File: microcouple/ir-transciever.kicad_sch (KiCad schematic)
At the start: 4 parts, among them U8 TSOP34138

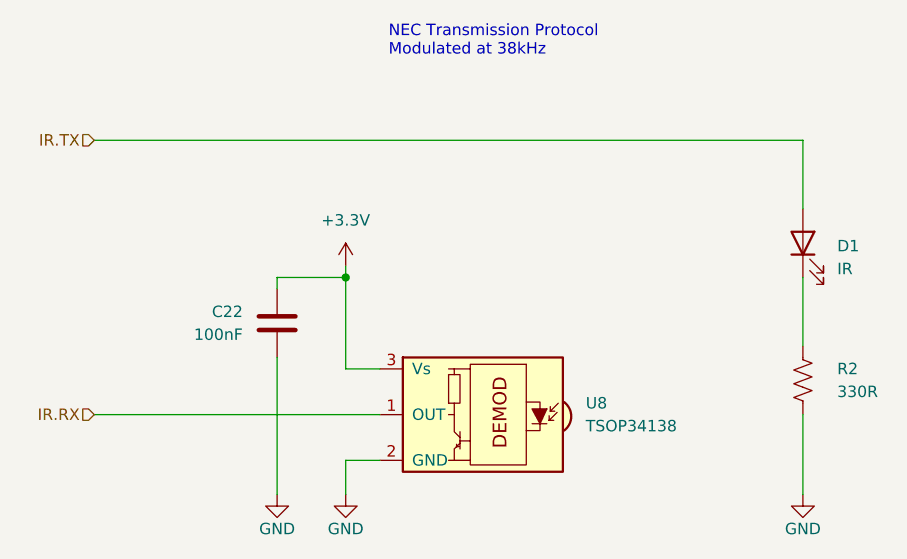
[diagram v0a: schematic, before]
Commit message: Switch THT IR components to SMD ones
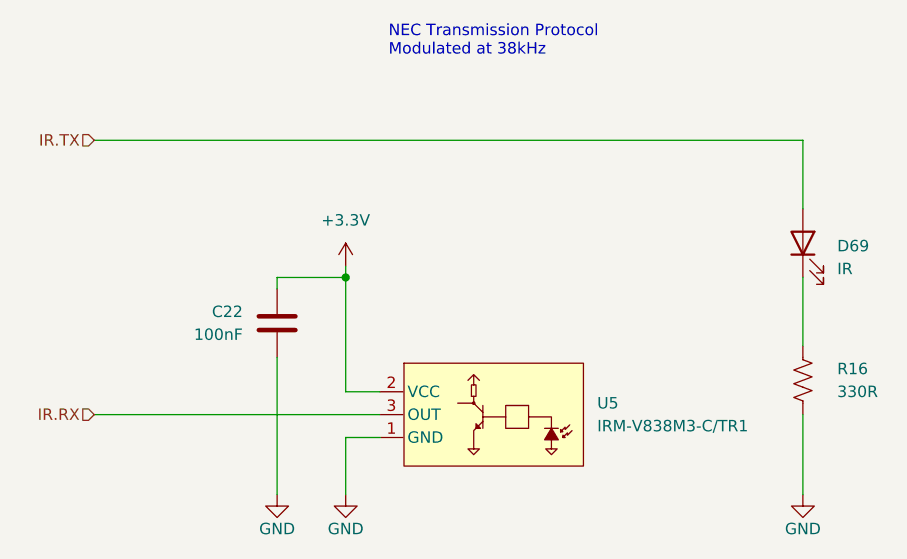
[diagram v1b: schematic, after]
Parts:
- removed U8: TSOP34138, OptoDevice:Vishay_MOLD-3Pin, symbol Interface_Optical:TSOP341xx
- added U5: IRM-V838M3-C/TR1, easyeda2kicad:OPTO-SMD_IRM-V838M3-C-TR1, symbol GS_Optoelectronic:IRM-V838M3-C_TR1
- D69: renamed from D1; footprint LED_THT:LED_SideEmitter_Rectangular_W4.5mm_H1.6mm -> easyeda2kicad:LED-SMD_L3.0-W2.7-RD; LCSC ID (none) -> C181893
- renumbered R2 to R16
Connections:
- net +3.3V: now also U5.2 (VCC)
- net GND: now also U5.1 (GND), U5.4 (GND)
- net IR.RX: now also U5.3 (OUT)
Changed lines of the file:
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@@
 	(wire
 		(pts
-			(xy 71.12 83.82) (xy 74.93 83.82)
-		)
-		(stroke
-			(width 0)
-			(type default)
-		)
-	)
-	(wire
-		(pts
-			(xy 71.12 87.63) (xy 71.12 83.82)
+			(xy 71.12 81.28) (xy 74.93 81.28)
+		)
+		(stroke
+			(width 0)
+			(type default)
+		)
+	)
+	(wire
+		(pts
+			(xy 71.12 87.63) (xy 71.12 81.28)
 		)
 		(stroke
@@
 	(wire
 		(pts
-			(xy 71.12 63.5) (xy 71.12 73.66)
+			(xy 71.12 63.5) (xy 71.12 76.2)
 		)
 		(stroke
@@
 	(wire
 		(pts
-			(xy 71.12 73.66) (xy 74.93 73.66)
+			(xy 71.12 76.2) (xy 74.93 76.2)
 		)
 		(stroke
@@
 	)
 	(symbol
+		(lib_id "GS_Optoelectronic:IRM-V838M3-C_TR1")
+		(at 81.28 77.47 0)
+		(unit 1)
+		(exclude_from_sim no)
+		(in_bom yes)
+		(on_board yes)
+		(dnp no)
+		(fields_autoplaced yes)
+		(property "Reference" "U5"
+			(at 99.06 77.4699 0)
+			(effects
+				(font
+					(size 1.27 1.27)
+				)
+				(justify left)
+			)
+		)
+		(property "Value" "IRM-V838M3-C/TR1"
+			(at 99.06 80.0099 0)
+			(effects
+				(font
+					(size 1.27 1.27)
+				)
+				(justify left)
+			)
+		)
+		(property "Footprint" "easyeda2kicad:OPTO-SMD_IRM-V838M3-C-TR1"
+			(at 81.28 88.9 0)
+			(effects
+				(font
+					(size 1.27 1.27)
+				)
+				(hide yes)
+			)
+		)
+		(property "Datasheet" ""
+			(at 81.28 77.47 0)
+			(effects
+				(font
+					(size 1.27 1.27)
+				)
+				(hide yes)
+			)
+		)
+		(property "Description" ""
+			(at 81.28 77.47 0)
+			(effects
+				(font
+					(size 1.27 1.27)
+				)
+				(hide yes)
+			)
+		)
+		(property "LCSC Part" "C3291489"
+			(at 81.28 91.44 0)
+			(effects
+				(font
+					(size 1.27 1.27)
+				)
+				(hide yes)
+			)
+		)
+		(pin "2"
+		)
+		(pin "3"
+		)
+		(pin "4"
+		)
+		(pin "1"
+		)
+		(instances
+			(project ""
+				(path "/d639f16d-aedb-4af6-af94-94ea25244267/6409c937-888b-495c-b718-919d7d6f3ec9"
+					(reference "U5")
+					(unit 1)
+				)
+			)
+		)
+	)
+	(symbol
 		(lib_id "power:GND")
 		(at 71.12 87.63 0)
@@
 		(on_board yes)
 		(dnp no)
-		(property "Reference" "#PWR073"
+		(property "Reference" "#PWR072"
 			(at 71.12 93.98 0)
 			(effects
@@
 			(project "microcouple"
 				(path "/d639f16d-aedb-4af6-af94-94ea25244267/6409c937-888b-495c-b718-919d7d6f3ec9"
-					(reference "#PWR073")
+					(reference "#PWR072")
 					(unit 1)
 				)
@@
 		(on_board yes)
 		(dnp no)
-		(property "Reference" "#PWR071"
+		(property "Reference" "#PWR070"
 			(at 71.12 66.04 0)
 			(effects
@@
 			(project "microcouple"
 				(path "/d639f16d-aedb-4af6-af94-94ea25244267/6409c937-888b-495c-b718-919d7d6f3ec9"
-					(reference "#PWR071")
-					(unit 1)
-				)
-			)
-		)
-	)
-	(symbol
-		(lib_id "Interface_Optical:TSOP341xx")
-		(at 85.09 78.74 0)
-		(mirror y)
-		(unit 1)
-		(exclude_from_sim no)
-		(in_bom yes)
-		(on_board yes)
-		(dnp no)
-		(fields_autoplaced yes)
-		(property "Reference" "U8"
-			(at 97.79 77.4699 0)
-			(effects
-				(font
-					(size 1.27 1.27)
-				)
-				(justify right)
-			)
-		)
-		(property "Value" "TSOP34138"
-			(at 97.79 80.0099 0)
-			(effects
-				(font
-					(size 1.27 1.27)
-				)
-				(justify right)
-			)
-		)
-		(property "Footprint" "OptoDevice:Vishay_MOLD-3Pin"
-			(at 86.36 88.265 0)
-			(effects
-				(font
-					(size 1.27 1.27)
-				)
-				(hide yes)
-			)
-		)
-		(property "Datasheet" "https://www.lcsc.com/datasheet/lcsc_datasheet_2410121755_Vishay-Intertech-TSOP34138_C118303.pdf"
-			(at 68.58 71.12 0)
-			(effects
-				(font
-					(size 1.27 1.27)
-				)
-				(hide yes)
-			)
-		)
-		(property "Description" "IR Receiver Modules for Remote Control Systems"
-			(at 85.09 78.74 0)
-			(effects
-				(font
-					(size 1.27 1.27)
-				)
-				(hide yes)
-			)
-		)
-		(property "LCSC ID" "C118303"
-			(at 85.09 78.74 0)
-			(effects
-				(font
-					(size 1.27 1.27)
-				)
-				(hide yes)
-			)
-		)
-		(pin "1"
-		)
-		(pin "2"
-		)
-		(pin "3"
-		)
-		(instances
-			(project "microcouple"
-				(path "/d639f16d-aedb-4af6-af94-94ea25244267/6409c937-888b-495c-b718-919d7d6f3ec9"
-					(reference "U8")
+					(reference "#PWR070")
 					(unit 1)
 				)
@@
 		(on_board yes)
 		(dnp no)
-		(property "Reference" "#PWR074"
+		(property "Reference" "#PWR073"
 			(at 121.92 93.98 0)
 			(effects
@@
 			(project "microcouple"
 				(path "/d639f16d-aedb-4af6-af94-94ea25244267/6409c937-888b-495c-b718-919d7d6f3ec9"
-					(reference "#PWR074")
+					(reference "#PWR073")
 					(unit 1)
 				)
@@
 		(dnp no)
 		(fields_autoplaced yes)
-		(property "Reference" "D1"
+		(property "Reference" "D69"
 			(at 125.73 60.0074 90)
 			(effects
@@
 			)
 		)
-		(property "Footprint" "LED_THT:LED_SideEmitter_Rectangular_W4.5mm_H1.6mm"
+		(property "Footprint" "easyeda2kicad:LED-SMD_L3.0-W2.7-RD"
 			(at 121.92 59.69 0)
 			(effects
@@
 			)
 		)
+		(property "LCSC ID" "C181893"
+			(at 121.92 59.69 90)
+			(effects
+				(font
+					(size 1.27 1.27)
+				)
+				(hide yes)
+			)
+		)
 		(pin "2"
 		)
@@
 			(project ""
 				(path "/d639f16d-aedb-4af6-af94-94ea25244267/6409c937-888b-495c-b718-919d7d6f3ec9"
-					(reference "D1")
+					(reference "D69")
 					(unit 1)
 				)
@@
 		(on_board yes)
 		(dnp no)
-		(property "Reference" "#PWR072"
+		(property "Reference" "#PWR071"
 			(at 63.5 93.98 0)
 			(effects
@@
 			(project "microcouple"
 				(path "/d639f16d-aedb-4af6-af94-94ea25244267/6409c937-888b-495c-b718-919d7d6f3ec9"
-					(reference "#PWR072")
+					(reference "#PWR071")
 					(unit 1)
 				)
@@
 		(on_board yes)
 		(dnp no)
-		(property "Reference" "R2"
+		(property "Reference" "R16"
 			(at 125.73 73.66 0)
 			(effects
@@
 			(project "microcouple"
 				(path "/d639f16d-aedb-4af6-af94-94ea25244267/6409c937-888b-495c-b718-919d7d6f3ec9"
-					(reference "R2")
-					(unit 1)
-				)
+					(reference "R16")
+					(unit 1)
+				)

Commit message: Draft layout
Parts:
- renumbered C22 to C23, R16 to R17, U5 to U7
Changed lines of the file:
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@@
 		(dnp no)
 		(fields_autoplaced yes)
-		(property "Reference" "U5"
+		(property "Reference" "U7"
 			(at 99.06 77.4699 0)
 			(effects
@@
 			(project ""
 				(path "/d639f16d-aedb-4af6-af94-94ea25244267/6409c937-888b-495c-b718-919d7d6f3ec9"
-					(reference "U5")
+					(reference "U7")
 					(unit 1)
 				)
@@
 		(on_board yes)
 		(dnp no)
-		(property "Reference" "#PWR072"
+		(property "Reference" "#PWR077"
 			(at 71.12 93.98 0)
 			(effects
@@
 			(project "microcouple"
 				(path "/d639f16d-aedb-4af6-af94-94ea25244267/6409c937-888b-495c-b718-919d7d6f3ec9"
-					(reference "#PWR072")
+					(reference "#PWR077")
 					(unit 1)
 				)
@@
 		(on_board yes)
 		(dnp no)
-		(property "Reference" "#PWR070"
+		(property "Reference" "#PWR076"
 			(at 71.12 66.04 0)
 			(effects
@@
 			(project "microcouple"
 				(path "/d639f16d-aedb-4af6-af94-94ea25244267/6409c937-888b-495c-b718-919d7d6f3ec9"
-					(reference "#PWR070")
+					(reference "#PWR076")
 					(unit 1)
 				)
@@
 		(on_board yes)
 		(dnp no)
-		(property "Reference" "#PWR073"
+		(property "Reference" "#PWR078"
 			(at 121.92 93.98 0)
 			(effects
@@
 			(project "microcouple"
 				(path "/d639f16d-aedb-4af6-af94-94ea25244267/6409c937-888b-495c-b718-919d7d6f3ec9"
-					(reference "#PWR073")
+					(reference "#PWR078")
 					(unit 1)
 				)
@@
 		(on_board yes)
 		(dnp no)
-		(property "Reference" "#PWR071"
+		(property "Reference" "#PWR075"
 			(at 63.5 93.98 0)
 			(effects
@@
 			(project "microcouple"
 				(path "/d639f16d-aedb-4af6-af94-94ea25244267/6409c937-888b-495c-b718-919d7d6f3ec9"
-					(reference "#PWR071")
+					(reference "#PWR075")
 					(unit 1)
 				)
@@
 		(dnp no)
 		(fields_autoplaced yes)
-		(property "Reference" "C22"
+		(property "Reference" "C23"
 			(at 59.69 67.3099 0)
 			(effects
@@
 			(project "microcouple"
 				(path "/d639f16d-aedb-4af6-af94-94ea25244267/6409c937-888b-495c-b718-919d7d6f3ec9"
-					(reference "C22")
+					(reference "C23")
 					(unit 1)
 				)
@@
 		(on_board yes)
 		(dnp no)
-		(property "Reference" "R16"
+		(property "Reference" "R17"
 			(at 125.73 73.66 0)
 			(effects
@@
 			(project "microcouple"
 				(path "/d639f16d-aedb-4af6-af94-94ea25244267/6409c937-888b-495c-b718-919d7d6f3ec9"
-					(reference "R16")
-					(unit 1)
-				)
+					(reference "R17")
+					(unit 1)
+				)

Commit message: Finish Silkscreen
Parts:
- C23: footprint Capacitor_SMD:C_0201_0603Metric -> GS_SMD:0201_0603Metric
- R17: footprint Resistor_SMD:R_0201_0603Metric -> GS_SMD:0201_0603Metric
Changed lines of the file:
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@@
 			)
 		)
-		(property "Footprint" "Capacitor_SMD:C_0201_0603Metric"
+		(property "Footprint" "GS_SMD:0201_0603Metric"
 			(at 62.5348 72.39 0)
 			(effects
@@
 			)
 		)
-		(property "Footprint" "Resistor_SMD:R_0201_0603Metric"
+		(property "Footprint" "GS_SMD:0201_0603Metric"
 			(at 122.936 75.184 90)
 			(effects

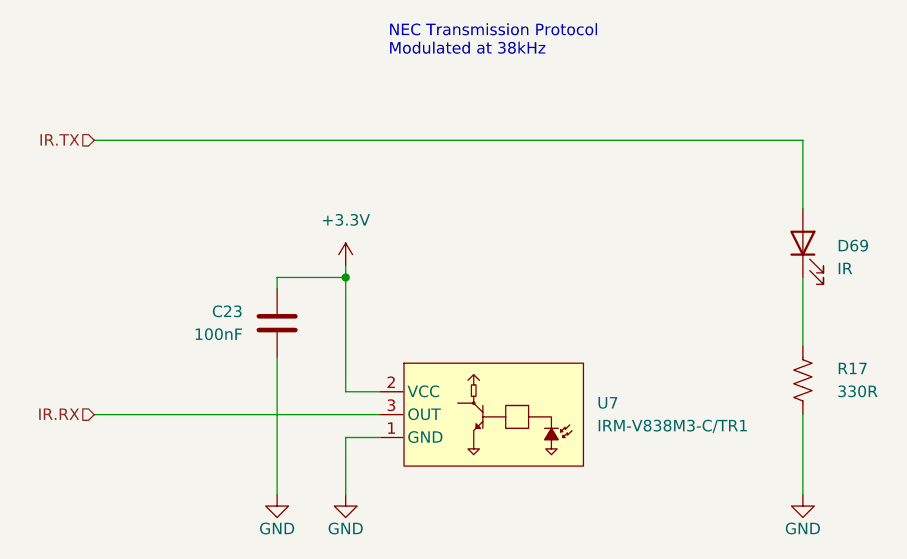
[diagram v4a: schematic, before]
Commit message: Update for JLCPCB
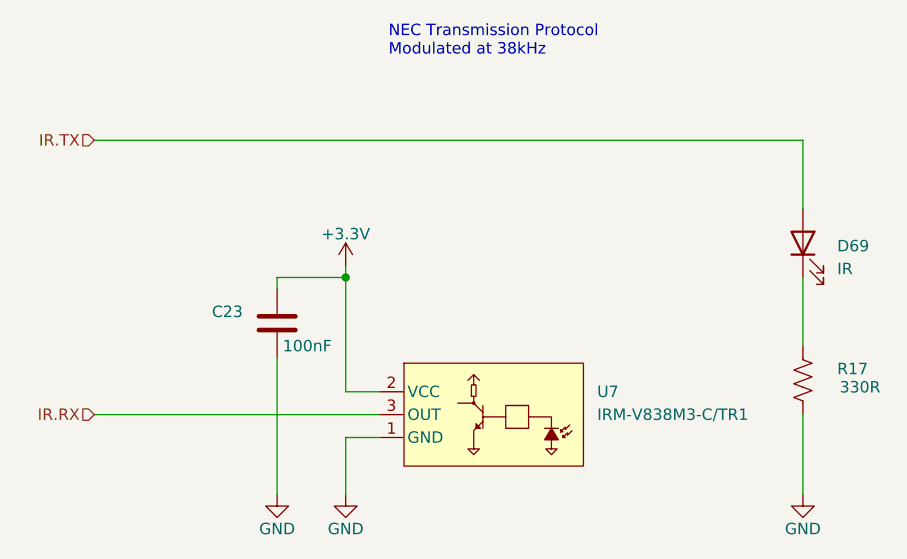
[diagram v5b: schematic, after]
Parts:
- C23: footprint GS_SMD:0201_0603Metric -> GS_Capacitors:C_0201_0603Metric; symbol Device:C -> GS_Capacitor_0201:C_0201_100nF; LCSC ID (none) -> C18164587; Manufacturer (none) -> CCTC; Mfr. Part # (none) -> TCC0201X5R104M250ZT; Package (none) -> 0201
- D69: symbol Device:LED -> GS_Optoelectronic:LED_2.7x3mm_IR_Horizontal; Manufacturer (none) -> Everlight Elec; Mfr. Part # (none) -> IR26-61C/L302/TR8; Package (none) -> SMD,2.7x3mm
- R17: footprint GS_SMD:0201_0603Metric -> GS_Resistors:R_0201_0603Metric; symbol Device:R_US -> GS_Resistor_0201:R_0201_330R; LCSC ID (none) -> C320833; Manufacturer (none) -> FH (Guangdong Fenghua Advanced Tech); Mfr. Part # (none) -> RC-01W3300FT; Package (none) -> 0201
- U7: LCSC ID (none) -> C3291489; LCSC Part C3291489 -> (none); Manufacturer (none) -> Everlight Elec; Mfr. Part # (none) -> IRM-V838M3-C/TR1; Package (none) -> SMD-4P,3x6.6mm
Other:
- title: (none) -> IR Transciever
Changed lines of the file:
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@@
 	(paper "A5")
 	(title_block
+		(title "IR Transciever")
+		(date "2025-04-27")
 		(rev "A")
 		(company "George Sleen")
@@
 		(fields_autoplaced yes)
 		(property "Reference" "U7"
-			(at 99.06 77.4699 0)
+			(at 99.06 76.1999 0)
 			(effects
 				(font
@@
 		)
 		(property "Value" "IRM-V838M3-C/TR1"
-			(at 99.06 80.0099 0)
+			(at 99.06 78.7399 0)
 			(effects
 				(font
@@
 			)
 		)
-		(property "Datasheet" ""
+		(property "Datasheet" "https://www.everlighteurope.com/custom/files/datasheets/DMO-0000605.pdf"
+			(at 81.026 60.452 0)
+			(effects
+				(font
+					(size 1.27 1.27)
+				)
+				(hide yes)
+			)
+		)
+		(property "Description" "Infrared Remote Receiver (IRM) 38kHz"
+			(at 81.026 62.992 0)
+			(effects
+				(font
+					(size 1.27 1.27)
+				)
+				(hide yes)
+			)
+		)
+		(property "Manufacturer" "Everlight Elec"
+			(at 81.28 56.388 0)
+			(effects
+				(font
+					(size 1.27 1.27)
+				)
+				(hide yes)
+			)
+		)
+		(property "Mfr. Part #" "IRM-V838M3-C/TR1"
+			(at 81.28 65.532 0)
+			(effects
+				(font
+					(size 1.27 1.27)
+				)
+				(hide yes)
+			)
+		)
+		(property "Package" "SMD-4P,3x6.6mm"
+			(at 81.28 58.674 0)
+			(effects
+				(font
+					(size 1.27 1.27)
+				)
+				(hide yes)
+			)
+		)
+		(property "LCSC ID" "C3291489"
+			(at 99.06 81.2799 0)
+			(effects
+				(font
+					(size 1.27 1.27)
+				)
+				(hide yes)
+			)
+		)
+		(property "LCSC Part" ""
 			(at 81.28 77.47 0)
 			(effects
@@
 					(size 1.27 1.27)
 				)
-				(hide yes)
-			)
-		)
-		(property "Description" ""
-			(at 81.28 77.47 0)
-			(effects
-				(font
-					(size 1.27 1.27)
-				)
-				(hide yes)
-			)
-		)
-		(property "LCSC Part" "C3291489"
-			(at 81.28 91.44 0)
-			(effects
-				(font
-					(size 1.27 1.27)
-				)
-				(hide yes)
 			)
 		)
@@
 		)
 		(property "Value" "+3.3V"
-			(at 71.12 57.15 0)
+			(at 71.12 58.674 0)
 			(effects
 				(font
@@
 	)
 	(symbol
-		(lib_id "Device:LED")
+		(lib_id "GS_Optoelectronic:LED_2.7x3mm_IR_Horizontal")
 		(at 121.92 59.69 90)
 		(unit 1)
@@
 		)
 		(property "Footprint" "easyeda2kicad:LED-SMD_L3.0-W2.7-RD"
+			(at 110.236 59.69 0)
+			(effects
+				(font
+					(size 1.27 1.27)
+				)
+				(hide yes)
+			)
+		)
+		(property "Datasheet" "https://www.everlighteurope.com/custom/files/datasheets/DIR-0000579.pdf"
+			(at 108.204 59.69 0)
+			(effects
+				(font
+					(size 1.27 1.27)
+				)
+				(hide yes)
+			)
+		)
+		(property "Description" "IR Light emitting diode"
+			(at 106.172 59.69 0)
+			(effects
+				(font
+					(size 1.27 1.27)
+				)
+				(hide yes)
+			)
+		)
+		(property "Sim.Pins" "1=K 2=A"
+			(at 99.568 60.96 0)
+			(effects
+				(font
+					(size 1.27 1.27)
+				)
+				(hide yes)
+			)
+		)
+		(property "LCSC ID" "C181893"
+			(at 104.648 59.69 0)
+			(effects
+				(font
+					(size 1.27 1.27)
+				)
+				(hide yes)
+			)
+		)
+		(property "Manufacturer" "Everlight Elec"
+			(at 101.092 59.69 0)
+			(effects
+				(font
+					(size 1.27 1.27)
+				)
+				(hide yes)
+			)
+		)
+		(property "Mfr. Part #" "IR26-61C/L302/TR8"
+			(at 102.87 59.69 0)
+			(effects
+				(font
+					(size 1.27 1.27)
+				)
+				(hide yes)
+			)
+		)
+		(property "Package" "SMD,2.7x3mm"
+			(at 98.044 59.69 0)
+			(effects
+				(font
+					(size 1.27 1.27)
+				)
+				(hide yes)
+			)
+		)
+		(property "LCSC Part" ""
 			(at 121.92 59.69 0)
 			(effects
@@
 					(size 1.27 1.27)
 				)
-				(hide yes)
-			)
-		)
-		(property "Datasheet" "~"
-			(at 121.92 59.69 0)
-			(effects
-				(font
-					(size 1.27 1.27)
-				)
-				(hide yes)
-			)
-		)
-		(property "Description" "Light emitting diode"
-			(at 121.92 59.69 0)
-			(effects
-				(font
-					(size 1.27 1.27)
-				)
-				(hide yes)
-			)
-		)
-		(property "Sim.Pins" "1=K 2=A"
-			(at 121.92 59.69 0)
-			(effects
-				(font
-					(size 1.27 1.27)
-				)
-				(hide yes)
-			)
-		)
-		(property "LCSC ID" "C181893"
-			(at 121.92 59.69 90)
-			(effects
-				(font
-					(size 1.27 1.27)
-				)
-				(hide yes)
 			)
 		)
@@
 	)
 	(symbol
-		(lib_id "Device:C")
+		(lib_id "GS_Capacitor_0201:C_0201_100nF")
 		(at 63.5 68.58 0)
-		(mirror y)
 		(unit 1)
 		(exclude_from_sim no)
@@
 		(on_board yes)
 		(dnp no)
-		(fields_autoplaced yes)
 		(property "Reference" "C23"
 			(at 59.69 67.3099 0)
@@
 					(size 1.27 1.27)
 				)
+				(justify right)
+			)
+		)
+		(property "Value" "100nF"
+			(at 64.135 71.12 0)
+			(effects
+				(font
+					(size 1.27 1.27)
+				)
 				(justify left)
 			)
 		)
-		(property "Value" "100nF"
-			(at 59.69 69.8499 0)
-			(effects
-				(font
-					(size 1.27 1.27)
-				)
-				(justify left)
-			)
-		)
-		(property "Footprint" "GS_SMD:0201_0603Metric"
-			(at 62.5348 72.39 0)
-			(effects
-				(font
-					(size 1.27 1.27)
-				)
-				(hide yes)
-			)
-		)
-		(property "Datasheet" "~"
+		(property "Footprint" "GS_Capacitors:C_0201_0603Metric"
+			(at 64.4652 72.39 0)
+			(effects
+				(font
+					(size 1.27 1.27)
+				)
+				(hide yes)
+			)
+		)
+		(property "Datasheet" "https://www.lcsc.com/datasheet/lcsc_datasheet_2410121315_CCTC-TCC0201X5R104M250ZT_C18164587.pdf"
 			(at 63.5 68.58 0)
 			(effects
@@
 				)
 				(hide yes)
+			)
+		)
+		(property "Manufacturer" "CCTC"
+			(at 63.5 68.58 0)
+			(effects
+				(font
+					(size 1.27 1.27)
+				)
+				(hide yes)
+			)
+		)
+		(property "Package" "0201"
+			(at 63.5 68.58 0)
+			(effects
+				(font
+					(size 1.27 1.27)
+				)
+				(hide yes)
+			)
+		)
+		(property "LCSC ID" "C18164587"
+			(at 63.5 68.58 0)
+			(effects
+				(font
+					(size 1.27 1.27)
+				)
+				(hide yes)
+			)
+		)
+		(property "Mfr. Part #" "TCC0201X5R104M250ZT"
+			(at 63.5 68.58 0)
+			(effects
+				(font
+					(size 1.27 1.27)
+				)
+				(hide yes)
+			)
+		)
+		(property "LCSC Part" ""
+			(at 63.5 68.58 0)
+			(effects
+				(font
+					(size 1.27 1.27)
+				)
 			)
 		)
@@
 	)
 	(symbol
-		(lib_id "Device:R_US")
+		(lib_id "GS_Resistor_0201:R_0201_330R")
 		(at 121.92 74.93 0)
 		(unit 1)
@@
 		)
 		(property "Value" "330R"
-			(at 125.73 76.2 0)
-			(effects
-				(font
-					(size 1.27 1.27)
-				)
-				(justify left)
-			)
-		)
-		(property "Footprint" "GS_SMD:0201_0603Metric"
-			(at 122.936 75.184 90)
-			(effects
-				(font
-					(size 1.27 1.27)
-				)
-				(hide yes)
-			)
-		)
-		(property "Datasheet" "~"
+			(at 128.27 75.692 0)
+			(effects
+				(font
+					(size 1.27 1.27)
+				)
+			)
+		)
+		(property "Footprint" "GS_Resistors:R_0201_0603Metric"
+			(at 121.92 52.832 0)
+			(effects
+				(font
+					(size 1.27 1.27)
+				)
+				(hide yes)
+			)
+		)
+		(property "Datasheet" "https://www.lcsc.com/datasheet/lcsc_datasheet_2411121005_FH--Guangdong-Fenghua-Advanced-Tech-RC-01W3300FT_C320833.pdf"
+			(at 121.92 57.404 0)
+			(effects
+				(font
+					(size 1.27 1.27)
+				)
+				(hide yes)
+			)
+		)
+		(property "Description" "Resistor, US symbol"
+			(at 121.92 48.26 0)
+			(effects
+				(font
+					(size 1.27 1.27)
+				)
+				(hide yes)
+			)
+		)
+		(property "Manufacturer" "FH (Guangdong Fenghua Advanced Tech)"
+			(at 121.92 55.118 0)
+			(effects
+				(font
+					(size 1.27 1.27)
+				)
+				(hide yes)
+			)
+		)
+		(property "Mfr. Part #" "RC-01W3300FT"
+			(at 121.92 50.292 0)
+			(effects
+				(font
+					(size 1.27 1.27)
+				)
+				(hide yes)
+			)
+		)
+		(property "LCSC ID" "C320833"
+			(at 121.92 46.228 0)
+			(effects
+				(font
+					(size 1.27 1.27)
+				)
+				(hide yes)
+			)
+		)
+		(property "Package" "0201"
+			(at 121.92 44.45 0)
+			(effects
+				(font
+					(size 1.27 1.27)
+				)
+				(hide yes)
+			)
+		)
+		(property "LCSC Part" ""
 			(at 121.92 74.93 0)
 			(effects
@@
 					(size 1.27 1.27)
 				)
-				(hide yes)
-			)
-		)
-		(property "Description" "Resistor, US symbol"
-			(at 121.92 74.93 0)
-			(effects
-				(font
-					(size 1.27 1.27)
-				)
-				(hide yes)
-			)
-		)
+			)
+		)
